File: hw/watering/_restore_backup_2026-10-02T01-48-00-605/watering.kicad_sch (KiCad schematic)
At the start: 7 parts, among them J2 USB_C_Receptacle

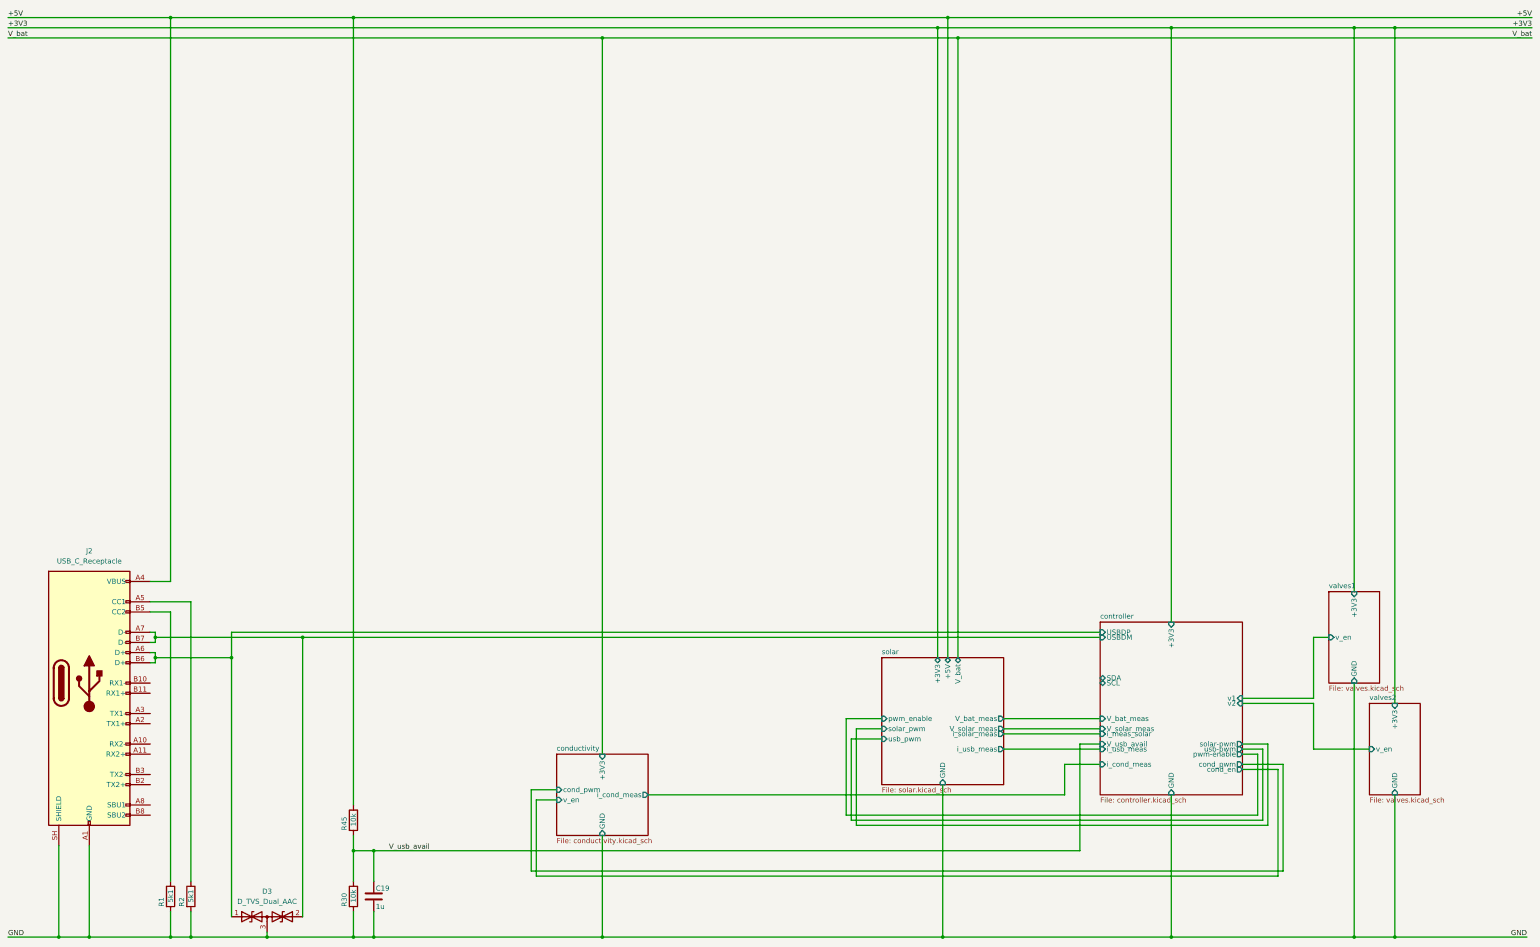
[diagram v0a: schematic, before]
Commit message: - sw   - charging batteries with solar somewhat works. mppt tracking is not possible because i messed up the current measurement   - implemented pid controller for current control. not operative, since current meas isn't working. maybe a voltage correlation is possibe? - hw   - current measurement is bad. output voltage of usb current is not high enough since input voltages are higher   - usb voltage wasn't connected correctly for charging   - solving by making battery voltage the main voltage bus on pcb and have all voltage users capped by switches to prevent battery drainage
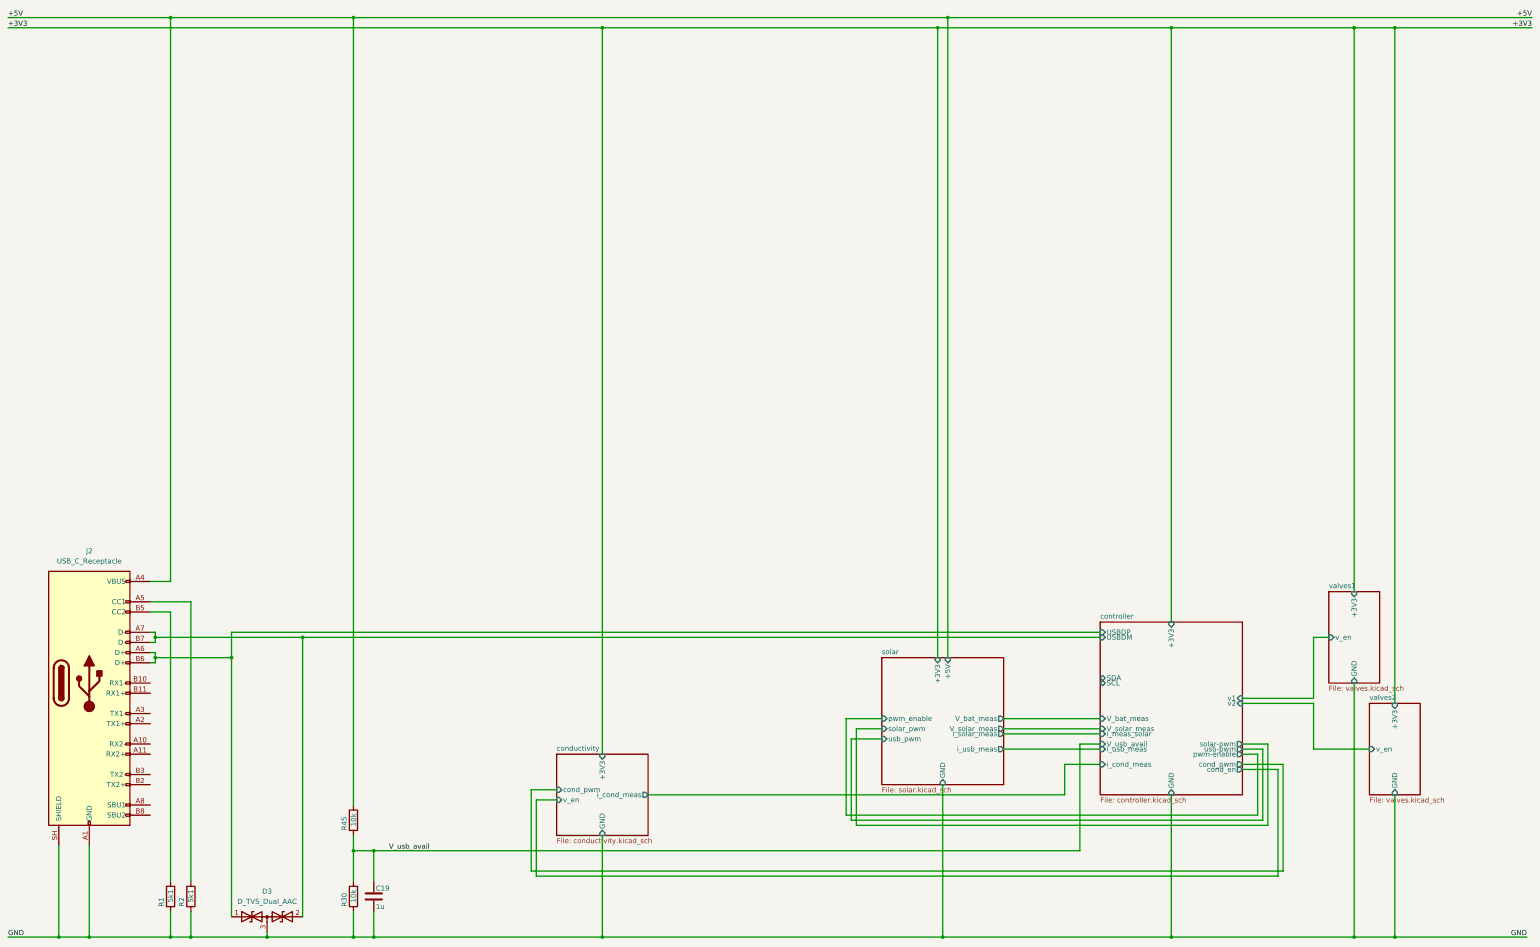
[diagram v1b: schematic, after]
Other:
- sheet solar ports: added none; removed V_bat
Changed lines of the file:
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@@
-	)
-	(junction
-		(at 259.08 24.13)
-		(diameter 0)
-		(color 0 0 0 0)
 	)
 	(junction
@@
 	)
 	(junction
-		(at 255.27 248.92)
+		(at 170.18 21.59)
 		(diameter 0)
 		(color 0 0 0 0)
 	)
 	(junction
-		(at 170.18 24.13)
+		(at 255.27 248.92)
 		(diameter 0)
 		(color 0 0 0 0)
@@
 	(wire
 		(pts
-			(xy 259.08 179.07) (xy 259.08 24.13)
-		)
-		(stroke
-			(width 0)
-			(type default)
-		)
-	)
-	(wire
-		(pts
 			(xy 233.68 220.98) (xy 233.68 196.85)
 		)
@@
 	(wire
 		(pts
-			(xy 170.18 24.13) (xy 259.08 24.13)
-		)
-		(stroke
-			(width 0)
-			(type default)
-		)
-	)
-	(wire
-		(pts
 			(xy 67.31 242.57) (xy 67.31 248.92)
 		)
@@
 	(wire
 		(pts
-			(xy 170.18 203.2) (xy 170.18 24.13)
+			(xy 170.18 203.2) (xy 170.18 21.59)
 		)
 		(stroke
@@
 	(wire
 		(pts
-			(xy 21.59 24.13) (xy 170.18 24.13)
-		)
-		(stroke
-			(width 0)
-			(type default)
-		)
-	)
-	(wire
-		(pts
 			(xy 95.25 173.99) (xy 95.25 243.84)
 		)
@@
 		(pts
 			(xy 358.14 162.56) (xy 358.14 21.59)
-		)
-		(stroke
-			(width 0)
-			(type default)
-		)
-	)
-	(wire
-		(pts
-			(xy 259.08 24.13) (xy 402.59 24.13)
 		)
 		(stroke
@@
 		)
 	)
-	(label "V_bat"
-		(at 21.59 24.13 0)
-		(effects
-			(font
-				(size 1.27 1.27)
-			)
-			(justify left bottom)
-		)
-	)
 	(label "V_usb_avail"
 		(at 127 227.33 180)
@@
 	(label "+3V3"
 		(at 402.59 21.59 180)
-		(effects
-			(font
-				(size 1.27 1.27)
-			)
-			(justify right bottom)
-		)
-	)
-	(label "V_bat"
-		(at 402.59 24.13 180)
 		(effects
 			(font
@@
 			)
 		)
-		(pin "+3V3" bidirectional
+		(pin "+3V3" input
 			(at 254 179.07 90)
 			(effects
@@
 			)
 		)
-		(pin "+5V" bidirectional
+		(pin "+5V" input
 			(at 256.54 179.07 90)
 			(effects
@@
 			)
 		)
-		(pin "V_bat" bidirectional
-			(at 259.08 179.07 90)
-			(effects
-				(font
-					(size 1.27 1.27)
-				)
-				(justify right)
-			)
-		)
